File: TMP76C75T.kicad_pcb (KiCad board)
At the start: 2 copper layers, 116.8 x 91.4 mm, 48 parts, among them J1 Conn_01x08_Male, J2 Conn_01x07_Male, J3 Conn_01x08_Male, J3-2 Conn_01x08_Male, J4 Conn_01x08_Male, J4-2 Conn_01x08_Male, J4-ADDR1 Conn_01x08_Male, J5 Conn_01x08_Male, J6 Conn_01x06_Male, J7 Conn_01x08_Male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

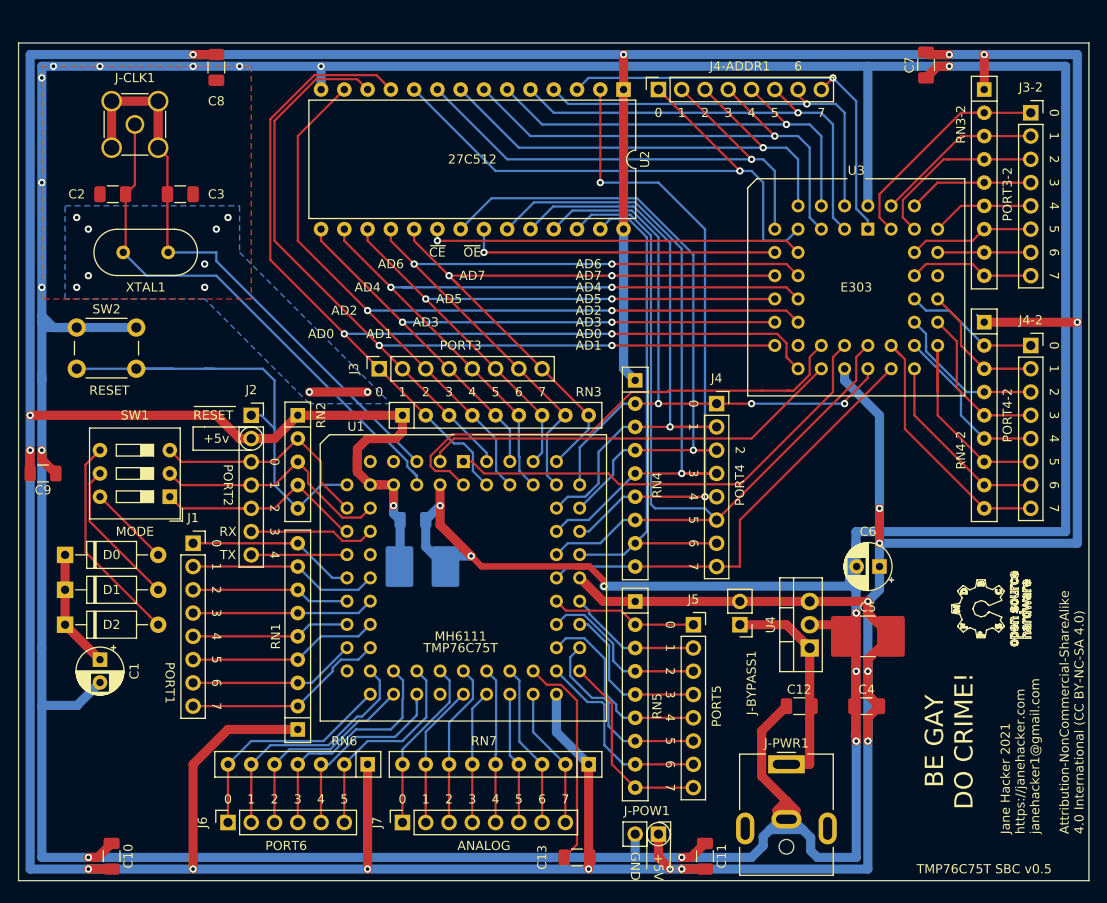
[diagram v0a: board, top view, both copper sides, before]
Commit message: Fixes and nice updates
Fixed power rails for M303, fixed reset line tied to cap, added ground headers, adde clock header
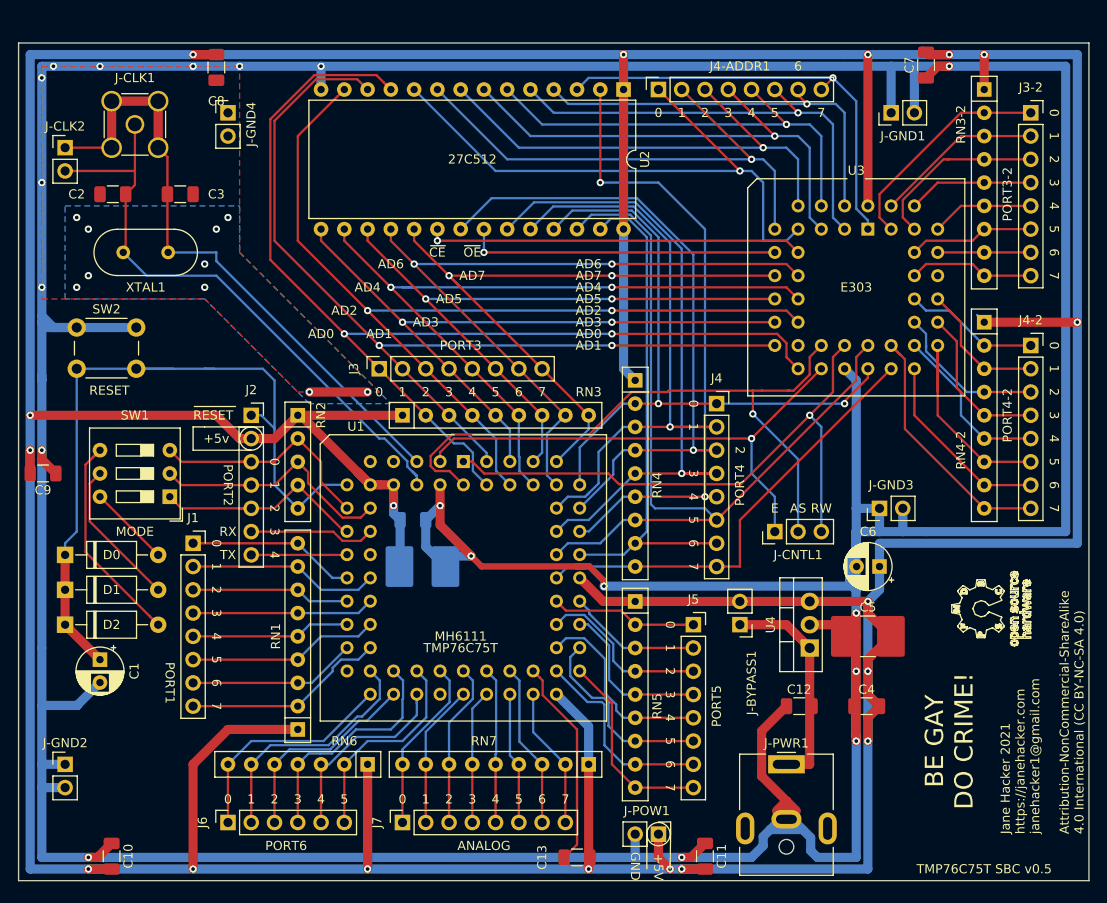
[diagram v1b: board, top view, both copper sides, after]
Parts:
- added J-CLK2: Conn_01x02_Male, Connector_PinHeader_2.54mm:PinHeader_1x02_P2.54mm_Vertical, F.Cu at (88.9, 63.5)
- added J-CNTL1: Conn_01x03_Male, Connector_PinHeader_2.54mm:PinHeader_1x03_P2.54mm_Vertical, F.Cu at (166.4, 105.4)
- added J-GND1: Conn_01x02, Connector_PinHeader_2.54mm:PinHeader_1x02_P2.54mm_Vertical, F.Cu at (179.1, 59.7)
- added J-GND2: Conn_01x02, Connector_PinHeader_2.54mm:PinHeader_1x02_P2.54mm_Vertical, F.Cu at (88.9, 130.8)
- added J-GND3: Conn_01x02, Connector_PinHeader_2.54mm:PinHeader_1x02_P2.54mm_Vertical, F.Cu at (177.8, 102.9)
- added J-GND4: Conn_01x02, Connector_PinHeader_2.54mm:PinHeader_1x02_P2.54mm_Vertical, F.Cu at (106.7, 59.7)
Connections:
- C1 pad 1: Net-(C1-Pad1) -> /RESET
- D0 pad 1: Net-(C1-Pad1) -> /RESET
- D1 pad 1: Net-(C1-Pad1) -> /RESET
- D2 pad 1: Net-(C1-Pad1) -> /RESET
- U3 pad 22: +5V -> GND
- U3 pad 44: GND -> +5V
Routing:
- net /RESET: track 51.9 -> 85.7 mm
- net GND: track 657.4 -> 684.6 mm
- net /AS: track 54.6 -> 72.0 mm, vias 0 -> 1
- net /RW: track 51.1 -> 64.4 mm, vias 0 -> 1
- net Net-(C1-Pad1): track 13.0 -> 0.00 mm
- net /E: track 46.4 -> 57.6 mm, vias 0 -> 1
- net /CLK2: track 58.7 -> 66.3 mm
- net /CLK1: track 64.3 -> 69.4 mm
- net +5V: track 694.1 -> 689.3 mm, vias 19 -> 18
- net /AN-: track 23.8 -> 22.9 mm
- net /A8: track 71.3 -> 71.6 mm, vias 3 -> 2
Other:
- board text added: "AS"
- board text added: "E"
- board text added: "RW"

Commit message: Updates
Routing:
- net +5V: track 689.3 -> 666.3 mm, vias 18 -> 17
- net /AS: track 72.0 -> 54.3 mm, vias 1 -> 0
- net GND: track 684.6 -> 678.7 mm, vias 28 -> 27
- net /A9: track 66.6 -> 61.2 mm
- net /RESET: track 85.7 -> 80.6 mm
- net /P4.5: track 25.0 -> 19.9 mm
- net /A11: track 70.8 -> 67.0 mm
- net /VIN: track 26.5 -> 23.9 mm
- net /A10: track 71.7 -> 69.2 mm
- net /P2.2: track 24.6 -> 22.7 mm
- net /AD7: track 72.1 -> 70.3 mm, vias 2 -> 0
- net Net-(D2-Pad2): track 24.6 -> 23.0 mm
- net /P4.7: track 28.5 -> 27.1 mm
- net /P2.1: track 28.4 -> 27.1 mm
- net /P2.0: track 26.6 -> 25.4 mm
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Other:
- net class Default removed

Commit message: v1.0 Update!
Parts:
- removed J-POW1: Conn_01x02, Connector_PinHeader_2.54mm:PinHeader_1x02_P2.54mm_Vertical
- added D3: LED_Small, LED_THT:LED_D3.0mm, F.Cu at (178.4, 134.5)
- added J-CNTL2: Conn_01x02, Connector_PinHeader_2.54mm:PinHeader_1x02_P2.54mm_Vertical, F.Cu at (157.7, 86.4)
- added J-PWR2: Conn_01x02, Connector_PinHeader_2.54mm:PinHeader_1x02_P2.54mm_Vertical, F.Cu at (151.1, 138.4)
- added J-PWR3: USB_B_Micro, Connector_USB:USB_Micro-B_Wuerth_629105150521, F.Cu at (95.8, 138.7)
- added R1: R_Small_US, Resistor_THT:R_Axial_DIN0207_L6.3mm_D2.5mm_P2.54mm_Vertical, F.Cu at (178.7, 128.4)
- J-BYPASS1: value Conn_01x02 -> Conn_01x03; footprint Connector_PinHeader_2.54mm:PinHeader_1x02_P2.54mm_Vertical -> Connector_PinHeader_2.54mm:PinHeader_1x03_P2.54mm_Vertical
- J1, J3, J3-2, J4, J4-2, J4-ADDR1, J5, J7: footprint Connector_PinSocket_2.54mm:PinSocket_1x08_P2.54mm_Vertical -> Connector_PinHeader_2.54mm:PinHeader_1x08_P2.54mm_Vertical
- J2: footprint Connector_PinSocket_2.54mm:PinSocket_1x07_P2.54mm_Vertical -> Connector_PinHeader_2.54mm:PinHeader_1x07_P2.54mm_Vertical
- J6: footprint Connector_PinSocket_2.54mm:PinSocket_1x06_P2.54mm_Vertical -> Connector_PinHeader_2.54mm:PinHeader_1x06_P2.54mm_Vertical
- U2: footprint Package_DIP:DIP-28_W15.24mm -> Socket:DIP_Socket-28_W11.9_W12.7_W15.24_W17.78_W18.5_3M_228-1277-00-0602J
- moved J-GND1 14.8 mm to (193.2, 55.2)
- moved J4-ADDR1 12.7 mm to (166.4, 57.5)
- moved J-BYPASS1 9.26 mm to (170.0, 121.0), turned to -90 degrees
- moved C10 7.49 mm to (86.5, 141.0), turned to 180 degrees
- moved U4 6.87 mm to (164.1, 114.9), turned to 0 degrees
- moved C7 2.66 mm to (182.9, 51.8)
- moved C12 1.94 mm to (168.0, 126.1), turned to 180 degrees
- moved U2 1.65 mm to (149.9, 55.5)
- moved J-GND2 1.40 mm to (88.9, 129.4)
- moved D0 0.89 mm to (88.0, 108.0)
- moved D1 0.89 mm to (88.0, 111.8)
- moved D2 0.89 mm to (88.0, 115.6)
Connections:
- J-BYPASS1 pad 1: /VIN -> +5V
- J-BYPASS1 pad 2: +5V -> /VIN
- U1 pad 17: Net-(U1-Pad17) -> unconnected-(U1-Pad17)
- U1 pad 26: Net-(U1-Pad26) -> unconnected-(U1-Pad26)
- U1 pad 33: Net-(U1-Pad33) -> unconnected-(U1-Pad33)
- U1 pad 7: Net-(U1-Pad7) -> unconnected-(U1-Pad7)
- U1 pad 9: Net-(U1-Pad9) -> unconnected-(U1-Pad9)
- U3 pad 19: Net-(U3-Pad19) -> unconnected-(U3-Pad19)
- U3 pad 35: Net-(U3-Pad35) -> unconnected-(U3-Pad35)
- U4 pad 1: /VIN -> /VREG
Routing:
- net +5V: track 666.3 -> 711.6 mm, vias 17 -> 18
- net GND: track 678.7 -> 697.9 mm, vias 27 -> 29
- net /AS: track 54.3 -> 72.0 mm, vias 0 -> 1
- net /CE: track 41.2 -> 56.9 mm, vias 1 -> 2
- net /OE: track 34.3 -> 49.0 mm, vias 1 -> 2
- net /VIN: track 23.9 -> 10.6 mm
- net /A7: track 48.4 -> 60.6 mm, vias 1 -> 0
- net /A6: track 44.3 -> 52.8 mm
- net /VREG: track 0.00 -> 6.46 mm
- net /A5: track 50.1 -> 55.9 mm
- net Net-(D3-Pad2): track 0.00 -> 4.53 mm
- net /A4: track 49.4 -> 52.9 mm
- net /A0: track 65.6 -> 62.1 mm
- net /A12: track 69.4 -> 66.9 mm
- net /A14: track 55.8 -> 57.6 mm
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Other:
- board size 116.8 x 91.4 mm -> 116.8 x 94.1 mm
- board text added: "150Ω"
- board text added: "27C256"
- board text added: "DIR"
- board text added: "J-BYPASS1: DIR=Bypass v. reg (external 5v supply to J-PWR1) REG=Use v. reg (12-24v supply to J-PWR1)"
- board text added: "PWR"
- board text added: "PWR ONLY"
- board text added: "REG"
- board text added: "TMP76C75T SBC v1.0"
- board text removed: "27C512"
- board text removed: "TMP76C75T SBC v0.5"
